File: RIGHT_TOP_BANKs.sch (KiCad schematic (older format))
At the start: 8 parts, among them J401 CONN_01X35, U301 iCE40-HX4K-TQ144

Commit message: The schematic is now free of any ERC error. Not connected and power flags added. No more global power pins, hierarchical labels used for power connections. TODO list: -Check if all footpritns are already assigned. -Export a BOM list, and check if all part numbers are assigned. -Add leds and testpoints. -Make another branch, with the RAM connections to the left and right banks, so the ram could be located in the bottom layer and the FPGA in the top layer. -Reorder the connections of the current branch if necessary, do the placement of components and ground planes.
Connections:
- net labels added: ADC_0, ADC_1, ADC_10, ADC_11, ADC_12, ADC_13, ADC_14, ADC_15, ADC_16, ADC_17, ADC_2, ADC_3, ADC_4, ADC_5, ADC_6, ADC_7, ADC_8, ADC_9
- net labels removed: ADC0, ADC1, ADC10, ADC11, ADC12, ADC13, ADC14, ADC15, ADC16, ADC17, ADC2, ADC3, ADC4, ADC5, ADC6, ADC7, ADC8, ADC9
- wire segments 22 -> 21
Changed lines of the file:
@@
-	1    0    0    -1
-$EndComp
-$Comp
-L GNDD #PWR068
-U 1 1 58E15B5E
-P 3700 5450
-F 0 "#PWR068" H 3700 5200 50  0001 C CNN
-F 1 "GNDD" H 3700 5300 50  0000 C CNN
-F 2 "" H 3700 5450 50  0001 C CNN
-F 3 "" H 3700 5450 50  0001 C CNN
-	1    3700 5450
 	1    0    0    -1
 $EndComp
 Text Notes 3550 1600 0    60   ~ 12
 FPGA BANK 0\n(TOP BANK)
-$Comp
-L +3.3V #PWR069
-U 1 1 58E15B6E
-P 3050 5350
-F 0 "#PWR069" H 3050 5200 50  0001 C CNN
-F 1 "+3.3V" H 3050 5490 50  0000 C CNN
-F 2 "" H 3050 5350 50  0001 C CNN
-F 3 "" H 3050 5350 50  0001 C CNN
-	1    3050 5350
-	1    0    0    -1
-$EndComp
 $Comp
 L iCE40-HX4K-TQ144 U?
@@
 Text Label 6050 3700 0    60   ~ 0
 IOR_140
-$Comp
-L GNDD #PWR070
-U 1 1 58E16C66
-P 6200 5700
-F 0 "#PWR070" H 6200 5450 50  0001 C CNN
-F 1 "GNDD" H 6200 5550 50  0000 C CNN
-F 2 "" H 6200 5700 50  0001 C CNN
-F 3 "" H 6200 5700 50  0001 C CNN
-	1    6200 5700
-	1    0    0    -1
-$EndComp
-$Comp
-L +3.3V #PWR071
-U 1 1 58E16C6C
-P 6300 5300
-F 0 "#PWR071" H 6300 5150 50  0001 C CNN
-F 1 "+3.3V" H 6300 5440 50  0000 C CNN
-F 2 "" H 6300 5300 50  0001 C CNN
-F 3 "" H 6300 5300 50  0001 C CNN
-	1    6300 5300
-	1    0    0    -1
-$EndComp
 Text Notes 5150 1600 0    60   ~ 12
 FPGA BANK 1\n(RIGHT BANK)
@@
 	1    0    0    -1
 $EndComp
-Text Label 3300 2750 2    60   ~ 0
-ADC0
-Text Label 3300 2850 2    60   ~ 0
-ADC1
-Text Label 3300 2950 2    60   ~ 0
-ADC2
-Text Label 3300 3050 2    60   ~ 0
-ADC3
-Text Label 3300 3150 2    60   ~ 0
-ADC4
-Text Label 3300 3250 2    60   ~ 0
-ADC5
-Text Label 3300 3350 2    60   ~ 0
-ADC6
-Text Label 3300 3450 2    60   ~ 0
-ADC7
-Text Label 3300 3550 2    60   ~ 0
-ADC8
-Text Label 3300 3650 2    60   ~ 0
-ADC9
-Text Label 3300 3750 2    60   ~ 0
-ADC10
-Text Label 3300 3850 2    60   ~ 0
-ADC11
-Text Label 3300 3950 2    60   ~ 0
-ADC12
-Text Label 3300 4050 2    60   ~ 0
-ADC13
-Text Label 3300 4150 2    60   ~ 0
-ADC14
-Text Label 3300 4250 2    60   ~ 0
-ADC15
-Text Label 3300 4350 2    60   ~ 0
-ADC16
-Text Label 3300 4450 2    60   ~ 0
-ADC17
 $Comp
 L CONN_01X35 J401
@@
 	1    0    0    -1
 $EndComp
-Text Notes 2900 3000 2    60   ~ 0
+Text Notes 2400 3050 2    60   ~ 0
 Available pins for ADC connections
 Text Notes 2750 2300 2    60   ~ 0
@@
 $EndComp
 $Comp
-L +3.3V #PWR072
-U 1 1 58E821E1
-P 7200 5200
-F 0 "#PWR072" H 7200 5050 50  0001 C CNN
-F 1 "+3.3V" H 7200 5340 50  0000 C CNN
-F 2 "" H 7200 5200 50  0001 C CNN
-F 3 "" H 7200 5200 50  0001 C CNN
-	1    7200 5200
-	1    0    0    -1
-$EndComp
-$Comp
-L GNDD #PWR073
-U 1 1 58E82242
-P 7700 5650
-F 0 "#PWR073" H 7700 5400 50  0001 C CNN
-F 1 "GNDD" H 7700 5500 50  0000 C CNN
-F 2 "" H 7700 5650 50  0001 C CNN
-F 3 "" H 7700 5650 50  0001 C CNN
-	1    7700 5650
-	1    0    0    -1
-$EndComp
-$Comp
-L +3.3V #PWR074
-U 1 1 58E823AD
-P 6950 1600
-F 0 "#PWR074" H 6950 1450 50  0001 C CNN
-F 1 "+3.3V" H 6950 1740 50  0000 C CNN
-F 2 "" H 6950 1600 50  0001 C CNN
-F 3 "" H 6950 1600 50  0001 C CNN
-	1    6950 1600
-	1    0    0    -1
-$EndComp
-$Comp
 L C C405
 U 1 1 58E823D3
@@
 	1    0    0    -1
 $EndComp
-$Comp
-L GNDD #PWR075
-U 1 1 58E824C7
-P 7150 2000
-F 0 "#PWR075" H 7150 1750 50  0001 C CNN
-F 1 "GNDD" H 7150 1850 50  0000 C CNN
-F 2 "" H 7150 2000 50  0001 C CNN
-F 3 "" H 7150 2000 50  0001 C CNN
-	1    7150 2000
-	1    0    0    -1
-$EndComp
-$Comp
-L GNDD #PWR076
-U 1 1 58E82512
-P 7300 3500
-F 0 "#PWR076" H 7300 3250 50  0001 C CNN
-F 1 "GNDD" H 7300 3350 50  0000 C CNN
-F 2 "" H 7300 3500 50  0001 C CNN
-F 3 "" H 7300 3500 50  0001 C CNN
-	1    7300 3500
-	1    0    0    -1
-$EndComp
-Wire Wire Line
-	3550 5450 3800 5450
-Connection ~ 3700 5450
+Wire Wire Line
+	3050 5450 3800 5450
 Wire Wire Line
 	3550 5150 3800 5150
 Wire Wire Line
-	3300 4750 3300 5350
+	3300 4750 3300 5050
 Connection ~ 3300 4850
 Wire Wire Line
-	3700 5150 3700 5050
-Wire Wire Line
-	3700 5050 3300 5050
+	3700 5050 3700 5150
+Wire Wire Line
+	3050 5050 3700 5050
 Connection ~ 3300 5050
 Connection ~ 3700 5150
 Wire Wire Line
-	3300 5350 3050 5350
-Wire Wire Line
-	6050 5700 6300 5700
-Connection ~ 6200 5700
+	6050 5700 6650 5700
 Wire Wire Line
 	6050 5000 6050 5400
 Connection ~ 6050 5100
 Wire Wire Line
-	6300 5300 6300 5400
-Wire Wire Line
-	6300 5350 6050 5350
+	6050 5350 6650 5350
+Wire Wire Line
+	6300 5350 6300 5400
 Connection ~ 6050 5350
 Connection ~ 6300 5350
@@
 	1900 2700 2950 2700
 Wire Wire Line
-	7200 5200 7850 5200
+	7400 5200 7850 5200
 Connection ~ 7700 5200
 Wire Wire Line
-	7700 5500 7700 5650
-Wire Wire Line
-	7700 5600 7850 5600
+	7400 5600 7850 5600
 Wire Wire Line
 	7850 5600 7850 5300
@@
 	7150 1900 7150 2000
 Wire Wire Line
-	7150 2000 7850 2000
+	6950 2000 7850 2000
 Wire Wire Line
 	7300 3500 7850 3500
@@
 Text Notes 2550 4700 2    60   ~ 0
 RAM connections
+Text HLabel 3300 2750 0    60   BiDi ~ 12
+ADC_0
+Text HLabel 3300 2850 0    60   BiDi ~ 12
+ADC_1
+Text HLabel 3300 2950 0    60   BiDi ~ 12
+ADC_2
+Text HLabel 3300 3050 0    60   BiDi ~ 12
+ADC_3
+Text HLabel 3300 3150 0    60   BiDi ~ 12
+ADC_4
+Text HLabel 3300 3250 0    60   BiDi ~ 12
+ADC_5
+Text HLabel 3300 3350 0    60   BiDi ~ 12
+ADC_6
+Text HLabel 3300 3450 0    60   BiDi ~ 12
+ADC_7
+Text HLabel 3300 3550 0    60   BiDi ~ 12
+ADC_8
+Text HLabel 3300 3650 0    60   BiDi ~ 12
+ADC_9
+Text HLabel 3300 3750 0    60   BiDi ~ 12
+ADC_10
+Text HLabel 3300 3850 0    60   BiDi ~ 12
+ADC_11
+Text HLabel 3300 3950 0    60   BiDi ~ 12
+ADC_12
+Text HLabel 3300 4050 0    60   BiDi ~ 12
+ADC_13
+Text HLabel 3300 4150 0    60   BiDi ~ 12
+ADC_14
+Text HLabel 3300 4250 0    60   BiDi ~ 12
+ADC_15
+Text HLabel 3300 4350 0    60   BiDi ~ 12
+ADC_16
+Text HLabel 3300 4450 0    60   BiDi ~ 12
+ADC_17
+Text HLabel 3050 5050 0    60   Input ~ 12
++3.3V
+Text HLabel 7400 5200 0    60   Input ~ 12
++3.3V
+Text HLabel 6950 1600 0    60   Input ~ 12
++3.3V
+Text HLabel 6650 5350 2    60   Input ~ 12
++3.3V
+Text HLabel 3050 5450 0    60   Input ~ 12
+GNDD
+Connection ~ 3550 5450
+Text HLabel 6650 5700 2    60   Input ~ 12
+GNDD
+Connection ~ 6300 5700
+Text HLabel 7400 5600 0    60   Input ~ 12
+GNDD
+Wire Wire Line
+	7700 5600 7700 5500
+Text HLabel 7300 3500 0    60   Input ~ 12
+GNDD
+Text HLabel 6950 2000 0    60   Input ~ 12
+GNDD
+Connection ~ 7150 2000
 $EndSCHEMATC

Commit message: First netlist export
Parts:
- J401: footprint (none) -> Pin_Headers:Pin_Header_Straight_1x35_Pitch1.27mm
- U301: footprint (none) -> Housings_QFP:LQFP-144_20x20mm_Pitch0.5mm
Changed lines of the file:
@@
 F 0 "U301" H 3500 2300 60  0000 L CNN
 F 1 "iCE40-HX4K-TQ144" H 3500 2200 60  0000 L CNN
-F 2 "" H 3300 2050 60  0001 C CNN
+F 2 "Housings_QFP:LQFP-144_20x20mm_Pitch0.5mm" H 3300 2050 60  0001 C CNN
 F 3 "" H 3300 2050 60  0001 C CNN
 	2    3300 2050
@@
 F 0 "U301" H 6250 2350 60  0000 L CNN
 F 1 "iCE40-HX4K-TQ144" H 6250 2250 60  0000 L CNN
-F 2 "" H 6050 2100 60  0001 C CNN
+F 2 "Housings_QFP:LQFP-144_20x20mm_Pitch0.5mm" H 6050 2100 60  0001 C CNN
 F 3 "" H 6050 2100 60  0001 C CNN
 	3    6050 2100
@@
 F 0 "J401" H 8050 5400 50  0000 C CNN
 F 1 "CONN_01X35" V 8150 3600 50  0000 C CNN
-F 2 "" H 8050 3600 50  0001 C CNN
+F 2 "Pin_Headers:Pin_Header_Straight_1x35_Pitch1.27mm" H 8050 3600 50  0001 C CNN
 F 3 "" H 8050 3600 50  0001 C CNN
 	1    8050 3600

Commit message: Fist approach of board placement
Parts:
- added D401, D402, D403, D404, D405, D406, D407, D408: GREEN, LEDs:LED_0603, symbol LED_ALT
- added R401, R402, R403, R404, R405, R406, R407, R408: 680, Resistors_SMD:R_0603_HandSoldering, symbol R
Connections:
- wire segments 21 -> 46

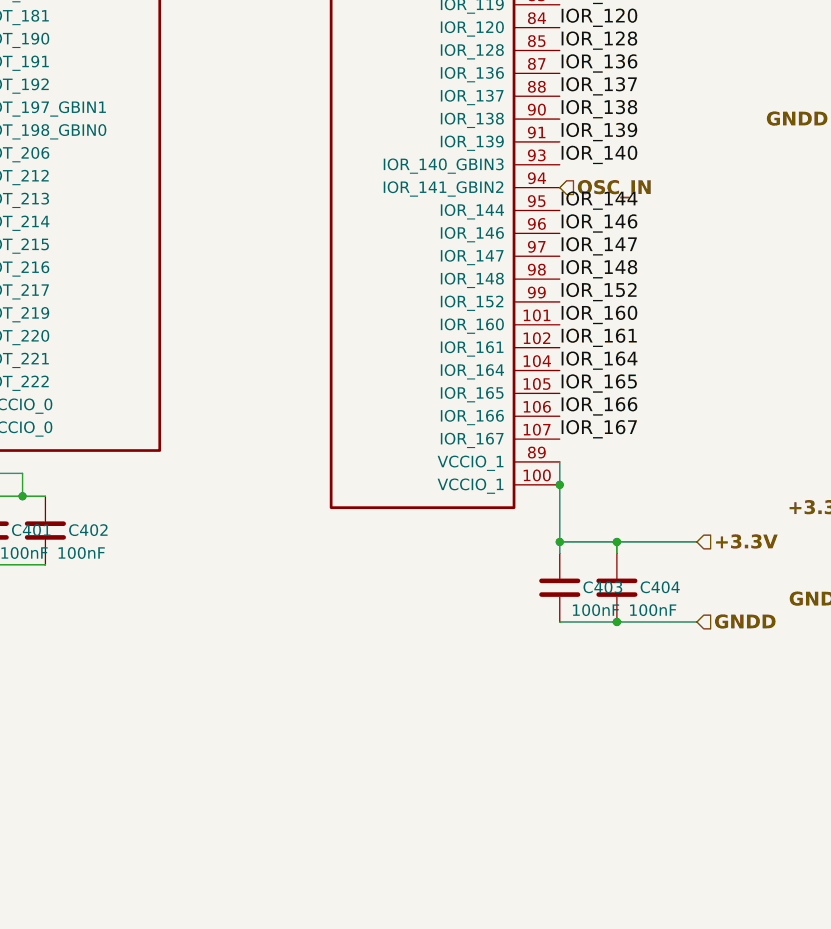
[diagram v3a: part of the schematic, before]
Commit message: Clk's buffers were removed and pcb routing was started
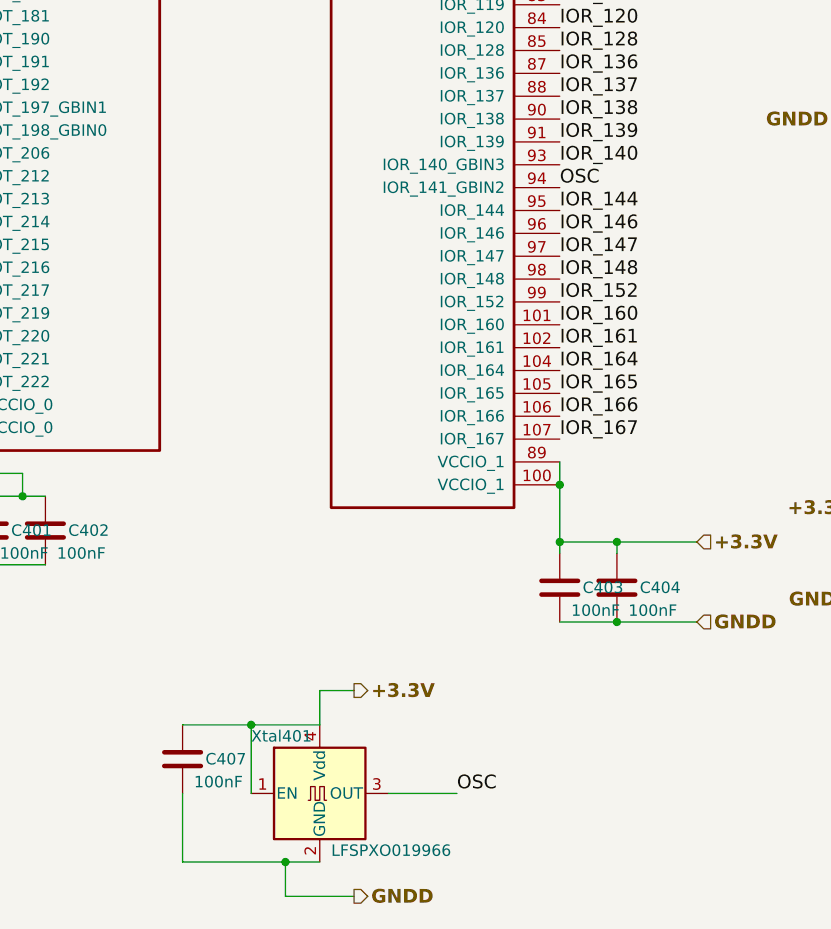
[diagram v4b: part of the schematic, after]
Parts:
- added C407: 100nF, Capacitors_SMD:C_0603_HandSoldering, symbol C
- added Xtal401: LFSPXO019966, Oscillators:Oscillator_SMD_Fordahl_DFAS11-4pin_7.0x5.0mm_HandSoldering, symbol LFSPXO019966
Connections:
- net labels added: OSC
- net labels removed: OSC_IN
- wire segments 46 -> 55
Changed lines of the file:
@@
 	7700 3500 7700 3700
 Connection ~ 7700 3500
-Text HLabel 6050 3800 2    60   Input ~ 12
-OSC_IN
 Text HLabel 3300 2050 0    60   BiDi ~ 12
 IOT_168
@@
 Text Label 9050 3200 2    60   ~ 0
 IOR_117
+$Comp
+L LFSPXO019966 Xtal401
+U 1 1 58F9ED80
+P 5000 6450
+F 0 "Xtal401" H 4700 6700 50  0000 L CNN
+F 1 "LFSPXO019966" H 5050 6200 50  0000 L CNN
+F 2 "Oscillators:Oscillator_SMD_Fordahl_DFAS11-4pin_7.0x5.0mm_HandSoldering" H 5700 6100 50  0001 C CNN
+F 3 "" H 4900 6450 50  0001 C CNN
+	1    5000 6450
+	1    0    0    -1
+$EndComp
+$Comp
+L C C407
+U 1 1 58F9ED8A
+P 4400 6300
+F 0 "C407" H 4500 6300 50  0000 L CNN
+F 1 "100nF" H 4450 6200 50  0000 L CNN
+F 2 "Capacitors_SMD:C_0603_HandSoldering" H 4438 6150 50  0001 C CNN
+F 3 "http://www.mouser.com/ds/2/212/KEM_C1002_X7R_SMD-357932.pdf" H 4400 6300 50  0001 C CNN
+F 4 "C0603C104K3RACTU" H 4400 6300 60  0001 C CNN "Manufacturer Part"
+F 5 "X7R" H 4400 6300 60  0001 C CNN "Dielectric"
+F 6 "25V (min. 10V)" H 4400 6300 60  0001 C CNN "VDC"
+	1    4400 6300
+	1    0    0    -1
+$EndComp
+Text HLabel 5150 6000 2    60   Output ~ 12
++3.3V
+Text HLabel 5150 6900 2    60   Output ~ 12
+GNDD
+Wire Wire Line
+	4700 6450 4700 6150
+Wire Wire Line
+	4400 6150 5000 6150
+Wire Wire Line
+	4400 6450 4400 6750
+Wire Wire Line
+	4400 6750 5000 6750
+Connection ~ 4700 6150
+Wire Wire Line
+	5000 6150 5000 6000
+Wire Wire Line
+	5000 6000 5150 6000
+Wire Wire Line
+	4850 6900 5150 6900
+Wire Wire Line
+	4850 6900 4850 6750
+Connection ~ 4850 6750
+Wire Wire Line
+	5300 6450 5600 6450
+Text Label 6050 3800 0    60   ~ 0
+OSC
+Text Label 5600 6450 0    60   ~ 0
+OSC
 $EndSCHEMATC

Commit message: Se conecta la tensión 5V a los conectores (right y left) y se cambia de nombre de un componente MIC2005A-2 -> MIC2005A-2YM5
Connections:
- net labels added: +5V
- wire segments 55 -> 57
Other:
- moved on the sheet: C405
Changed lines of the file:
@@
 LIBS:MIC2005A-2
 LIBS:AS4C1M16S
-LIBS:iCE40hxk4_dev_board-cache
 EELAYER 25 0
 EELAYER END
@@
 Text Notes 5150 1600 0    60   ~ 12
 FPGA BANK 1\n(RIGHT BANK)
-Text Notes 7150 1550 0    60   ~ 12
+Text Notes 7150 1450 0    60   ~ 12
 RIGHT HEADER
 Text Label 6050 2400 0    60   ~ 0
@@
 Text Notes 2750 2300 2    60   ~ 0
 TO LEFT CONNECTOR
+Text Label 7850 3800 2    60   ~ 0
+IOR_139
+Text Label 7850 3700 2    60   ~ 0
+IOR_138
+Text Label 7850 3500 2    60   ~ 0
+IOR_137
+Text Label 7850 4100 2    60   ~ 0
+IOR_146
+Text Label 7850 4000 2    60   ~ 0
+IOR_144
 Text Label 7850 3900 2    60   ~ 0
-IOR_139
-Text Label 7850 3800 2    60   ~ 0
-IOR_138
+IOR_140
+Text Label 7850 2500 2    60   ~ 0
+IOR_112
+Text Label 7850 2400 2    60   ~ 0
+IOR_111
+Text Label 7850 2300 2    60   ~ 0
+IOR_110
+Text Label 7850 2200 2    60   ~ 0
+IOR_109
+Text Label 7850 2900 2    60   ~ 0
+IOR_117
+Text Label 7850 2800 2    60   ~ 0
+IOR_116
+Text Label 7850 2700 2    60   ~ 0
+IOR_115
+Text Label 7850 2600 2    60   ~ 0
+IOR_114
+Text Label 7850 3300 2    60   ~ 0
+IOR_128
+Text Label 7850 3200 2    60   ~ 0
+IOR_120
+Text Label 7850 3100 2    60   ~ 0
+IOR_119
+Text Label 7850 3000 2    60   ~ 0
+IOR_118
 Text Label 7850 3400 2    60   ~ 0
-IOR_137
+IOR_136
 Text Label 7850 4200 2    60   ~ 0
-IOR_146
-Text Label 7850 4100 2    60   ~ 0
-IOR_144
-Text Label 7850 4000 2    60   ~ 0
-IOR_140
-Text Label 7850 2400 2    60   ~ 0
-IOR_112
-Text Label 7850 2300 2    60   ~ 0
-IOR_111
-Text Label 7850 2200 2    60   ~ 0
-IOR_110
-Text Label 7850 2100 2    60   ~ 0
-IOR_109
-Text Label 7850 2800 2    60   ~ 0
-IOR_117
-Text Label 7850 2700 2    60   ~ 0
-IOR_116
-Text Label 7850 2600 2    60   ~ 0
-IOR_115
-Text Label 7850 2500 2    60   ~ 0
-IOR_114
-Text Label 7850 3200 2    60   ~ 0
-IOR_128
-Text Label 7850 3100 2    60   ~ 0
-IOR_120
-Text Label 7850 3000 2    60   ~ 0
-IOR_119
-Text Label 7850 2900 2    60   ~ 0
-IOR_118
-Text Label 7850 3300 2    60   ~ 0
-IOR_136
+IOR_147
 Text Label 7850 4300 2    60   ~ 0
-IOR_147
+IOR_148
 Text Label 7850 4400 2    60   ~ 0
-IOR_148
+IOR_152
 Text Label 7850 4500 2    60   ~ 0
-IOR_152
+IOR_160
 Text Label 7850 4600 2    60   ~ 0
-IOR_160
+IOR_161
 Text Label 7850 4700 2    60   ~ 0
-IOR_161
+IOR_164
 Text Label 7850 4800 2    60   ~ 0
-IOR_164
+IOR_165
 Text Label 7850 4900 2    60   ~ 0
-IOR_165
+IOR_166
 Text Label 7850 5000 2    60   ~ 0
-IOR_166
-Text Label 7850 5100 2    60   ~ 0
 IOR_167
 $Comp
@@
 L C C405
 U 1 1 58E823D3
-P 7150 1750
-F 0 "C405" H 6900 1800 50  0000 L CNN
-F 1 "100nF" H 6800 1700 50  0000 L CNN
-F 2 "Capacitors_SMD:C_0603_HandSoldering" H 7188 1600 50  0001 C CNN
-F 3 "http://www.mouser.com/ds/2/212/KEM_C1002_X7R_SMD-357932.pdf" H 7150 1750 50  0001 C CNN
-F 4 "C0603C104K3RACTU" H 7150 1750 60  0001 C CNN "Manufacturer Part"
-F 5 "X7R" H 7150 1750 60  0001 C CNN "Dielectric"
-F 6 "25V (min. 10V)" H 7150 1750 60  0001 C CNN "VDC"
-	1    7150 1750
+P 7150 1850
+F 0 "C405" H 6900 1900 50  0000 L CNN
+F 1 "100nF" H 6800 1800 50  0000 L CNN
+F 2 "Capacitors_SMD:C_0603_HandSoldering" H 7188 1700 50  0001 C CNN
+F 3 "http://www.mouser.com/ds/2/212/KEM_C1002_X7R_SMD-357932.pdf" H 7150 1850 50  0001 C CNN
+F 4 "C0603C104K3RACTU" H 7150 1850 60  0001 C CNN "Manufacturer Part"
+F 5 "X7R" H 7150 1850 60  0001 C CNN "Dielectric"
+F 6 "25V (min. 10V)" H 7150 1850 60  0001 C CNN "VDC"
+	1    7150 1850
 	1    0    0    -1
 $EndComp
@@
 	7850 5600 7850 5300
 Connection ~ 7700 5600
-Wire Wire Line
-	6950 1600 7850 1600
-Wire Wire Line
-	7850 1600 7850 1900
-Connection ~ 7150 1600
-Wire Wire Line
-	7150 1900 7150 2000
-Wire Wire Line
-	6950 2000 7850 2000
-Wire Wire Line
-	7300 3500 7850 3500
-Wire Wire Line
-	7850 3600 7700 3600
-Wire Wire Line
-	7700 3500 7700 3700
-Connection ~ 7700 3500
+Connection ~ 7150 1700
+Wire Wire Line
+	7150 2000 7150 2100
+Wire Wire Line
+	6950 2100 7850 2100
 Text HLabel 3300 2050 0    60   BiDi ~ 12
 IOT_168
@@
 Text HLabel 3300 2650 0    60   BiDi ~ 12
 IOT_174
-Wire Wire Line
-	7700 3700 7850 3700
-Connection ~ 7700 3600
 Text HLabel 3300 4550 0    60   BiDi ~ 12
 DQ15
@@
 Text HLabel 7400 5200 0    60   Input ~ 12
 +3.3V
-Text HLabel 6950 1600 0    60   Input ~ 12
+Text HLabel 6950 1700 0    60   Input ~ 12
 +3.3V
 Text HLabel 6650 5350 2    60   Input ~ 12
@@
 Wire Wire Line
 	7700 5600 7700 5500
-Text HLabel 7300 3500 0    60   Input ~ 12
+Text HLabel 7300 3600 0    60   Input ~ 12
 GNDD
-Text HLabel 6950 2000 0    60   Input ~ 12
+Text HLabel 6950 2100 0    60   Input ~ 12
 GNDD
-Connection ~ 7150 2000
+Connection ~ 7150 2100
 $Comp
 L LED_ALT D401
@@
 Text Label 5600 6450 0    60   ~ 0
 OSC
+Wire Wire Line
+	7300 3600 7850 3600
+Wire Wire Line
+	6950 1700 7300 1700
+Wire Wire Line
+	7300 1700 7300 2000
+Wire Wire Line
+	7300 2000 7850 2000
+Text HLabel 6950 1600 0    60   Input ~ 12
++5V
+Wire Wire Line
+	6950 1600 7400 1600
+Wire Wire Line
+	7400 1600 7400 1900
+Wire Wire Line
+	7400 1900 7850 1900
+Text HLabel 7400 5100 0    60   Input ~ 12
++5V
+Wire Wire Line
+	7400 5100 7850 5100
 $EndSCHEMATC

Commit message: Ended placing (?)
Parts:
- removed C406: 100nF, Capacitors_SMD:C_0603_HandSoldering, symbol C
- removed J401: CONN_01X35, Pin_Headers:Pin_Header_Straight_1x35_Pitch1.27mm, symbol CONN_01X35
- added J401: CONN_01X20, Pin_Headers:Pin_Header_Straight_1x20_Pitch1.27mm, symbol CONN_01X20
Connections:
- wire segments 57 -> 51
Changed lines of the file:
@@
-	1    0    0    -1
-$EndComp
-$Comp
-L CONN_01X35 J401
-U 1 1 58E81FE2
-P 8050 3600
-F 0 "J401" H 8050 5400 50  0000 C CNN
-F 1 "CONN_01X35" V 8150 3600 50  0000 C CNN
-F 2 "Pin_Headers:Pin_Header_Straight_1x35_Pitch1.27mm" H 8050 3600 50  0001 C CNN
-F 3 "" H 8050 3600 50  0001 C CNN
-	1    8050 3600
 	1    0    0    -1
 $EndComp
@@
 Text Notes 2750 2300 2    60   ~ 0
 TO LEFT CONNECTOR
-Text Label 7850 3800 2    60   ~ 0
-IOR_139
-Text Label 7850 3700 2    60   ~ 0
-IOR_138
-Text Label 7850 3500 2    60   ~ 0
-IOR_137
-Text Label 7850 4100 2    60   ~ 0
-IOR_146
-Text Label 7850 4000 2    60   ~ 0
-IOR_144
-Text Label 7850 3900 2    60   ~ 0
-IOR_140
 Text Label 7850 2500 2    60   ~ 0
 IOR_112
@@
 Text Label 7850 2600 2    60   ~ 0
 IOR_114
-Text Label 7850 3300 2    60   ~ 0
-IOR_128
-Text Label 7850 3200 2    60   ~ 0
-IOR_120
-Text Label 7850 3100 2    60   ~ 0
-IOR_119
-Text Label 7850 3000 2    60   ~ 0
-IOR_118
-Text Label 7850 3400 2    60   ~ 0
-IOR_136
-Text Label 7850 4200 2    60   ~ 0
-IOR_147
-Text Label 7850 4300 2    60   ~ 0
-IOR_148
-Text Label 7850 4400 2    60   ~ 0
-IOR_152
-Text Label 7850 4500 2    60   ~ 0
-IOR_160
-Text Label 7850 4600 2    60   ~ 0
-IOR_161
-Text Label 7850 4700 2    60   ~ 0
-IOR_164
-Text Label 7850 4800 2    60   ~ 0
-IOR_165
-Text Label 7850 4900 2    60   ~ 0
-IOR_166
-Text Label 7850 5000 2    60   ~ 0
-IOR_167
-$Comp
-L C C406
-U 1 1 58E82127
-P 7700 5350
-F 0 "C406" H 7450 5400 50  0000 L CNN
-F 1 "100nF" H 7350 5300 50  0000 L CNN
-F 2 "Capacitors_SMD:C_0603_HandSoldering" H 7738 5200 50  0001 C CNN
-F 3 "http://www.mouser.com/ds/2/212/KEM_C1002_X7R_SMD-357932.pdf" H 7700 5350 50  0001 C CNN
-F 4 "C0603C104K3RACTU" H 7700 5350 60  0001 C CNN "Manufacturer Part"
-F 5 "X7R" H 7700 5350 60  0001 C CNN "Dielectric"
-F 6 "25V (min. 10V)" H 7700 5350 60  0001 C CNN "VDC"
-	1    7700 5350
-	1    0    0    -1
-$EndComp
 $Comp
 L C C405
@@
 Wire Notes Line
 	1900 2700 2950 2700
-Wire Wire Line
-	7400 5200 7850 5200
-Connection ~ 7700 5200
-Wire Wire Line
-	7400 5600 7850 5600
-Wire Wire Line
-	7850 5600 7850 5300
-Connection ~ 7700 5600
 Connection ~ 7150 1700
 Wire Wire Line
@@
 Text HLabel 3050 5050 0    60   Input ~ 12
 +3.3V
-Text HLabel 7400 5200 0    60   Input ~ 12
-+3.3V
 Text HLabel 6950 1700 0    60   Input ~ 12
-+3.3V
-Text HLabel 6650 5350 2    60   Input ~ 12
 +3.3V
 Text HLabel 3050 5450 0    60   Input ~ 12
 GNDD
 Connection ~ 3550 5450
-Text HLabel 6650 5700 2    60   Input ~ 12
-GNDD
 Connection ~ 6300 5700
-Text HLabel 7400 5600 0    60   Input ~ 12
-GNDD
-Wire Wire Line
-	7700 5600 7700 5500
-Text HLabel 7300 3600 0    60   Input ~ 12
-GNDD
 Text HLabel 6950 2100 0    60   Input ~ 12
 GNDD
@@
 OSC
 Wire Wire Line
-	7300 3600 7850 3600
-Wire Wire Line
 	6950 1700 7300 1700
 Wire Wire Line
@@
 Wire Wire Line
 	7400 1900 7850 1900
-Text HLabel 7400 5100 0    60   Input ~ 12
-+5V
-Wire Wire Line
-	7400 5100 7850 5100
+$Comp
+L CONN_01X20 J401
+U 1 1 59699B76
+P 8050 2850
+F 0 "J401" H 8050 3900 50  0000 C CNN
+F 1 "CONN_01X20" V 8150 2850 50  0000 C CNN
+F 2 "Pin_Headers:Pin_Header_Straight_1x20_Pitch1.27mm" H 8050 2850 50  0001 C CNN
+F 3 "" H 8050 2850 50  0001 C CNN
+	1    8050 2850
+	1    0    0    -1
+$EndComp
+Text Label 7850 3700 2    60   ~ 0
+IOR_139
+Text Label 7850 3600 2    60   ~ 0
+IOR_138
+Text Label 7850 3500 2    60   ~ 0
+IOR_137
+Text Label 7850 3300 2    60   ~ 0
+IOR_128
+Text Label 7850 3200 2    60   ~ 0
+IOR_120
+Text Label 7850 3100 2    60   ~ 0
+IOR_119
+Text Label 7850 3000 2    60   ~ 0
+IOR_118
+Text Label 7850 3400 2    60   ~ 0
+IOR_136
+Text Label 7850 3800 2    60   ~ 0
+IOR_140
 $EndSCHEMATC
